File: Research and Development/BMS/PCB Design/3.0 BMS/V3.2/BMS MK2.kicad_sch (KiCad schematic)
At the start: 40 parts, among them J13 CHG VCCs, J4 Batt +, J7 Batt -, J9 CHG GND, Q1 AO3400A, Q2 PN100, Q4 IRF9540N, Q5 IRF9540N, SW1 SW_SPST, SW2 SW_SPST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

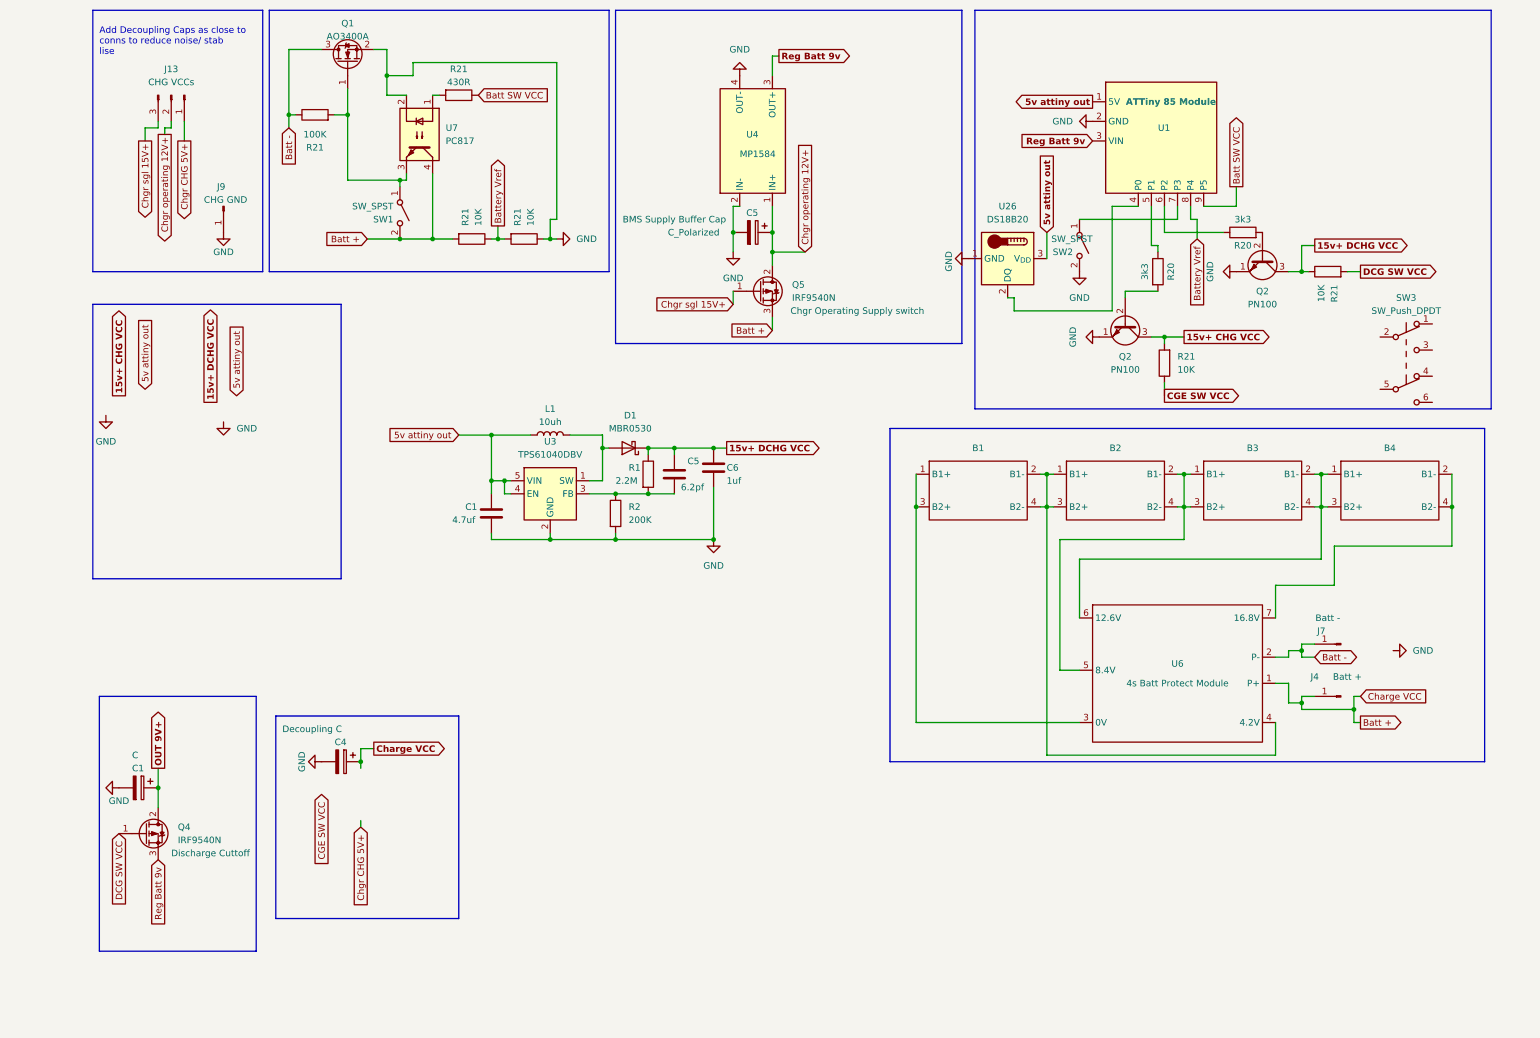
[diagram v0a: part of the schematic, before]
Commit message: Finalised BMS  schematic befeore testing PCB
is rough design without considering guitar dimension, little EMI considerations. not all concepts in design have been ensured to work properly. will test each sections viability before testing entire Circuit.

first design with the batterys and the circuit on the same board. initially had the idea of a 3d printed holder for the cells and a board on top.
 then 3 layers of single sided pcbs triple deckered with smd battery mounts. finally to this style.
although the board is larger in width and length, the height is reduced which should permit a slot in battery design for the guitar rather than a large module with a rail on the side of the guitar for battery to connect to.
This should make the design simpler and will look nicer becasue there will only be a small plastic plate exposed, rather than a chunk of the guitar body being plastic, ruining the over all finish of the guitar.
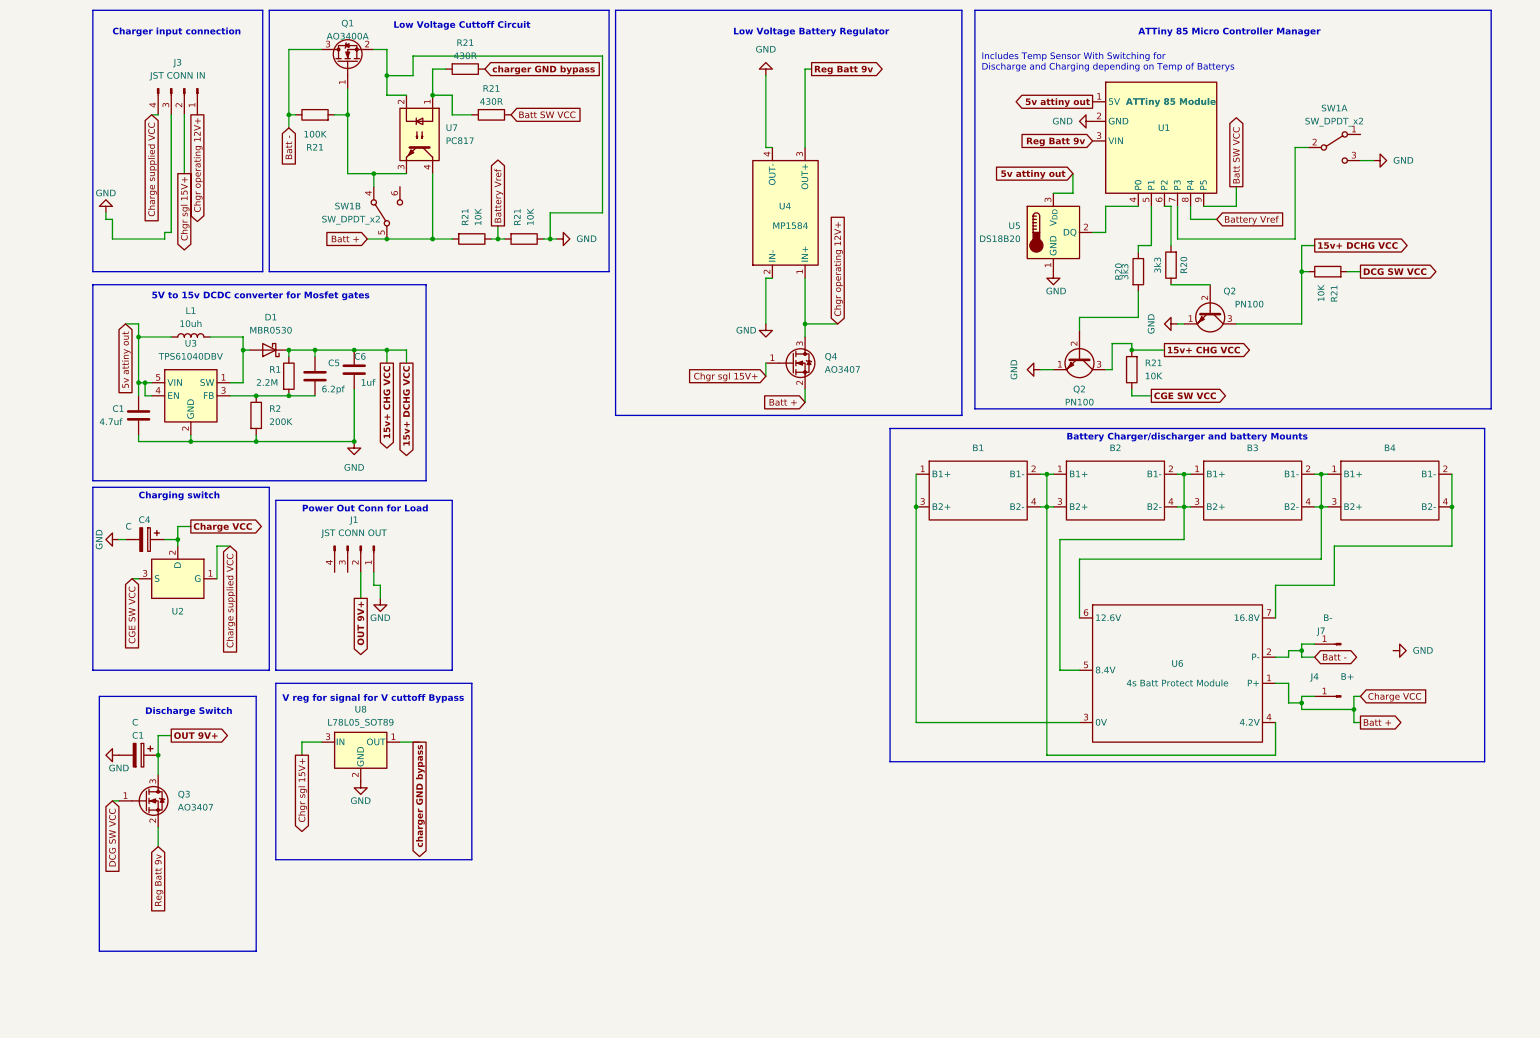
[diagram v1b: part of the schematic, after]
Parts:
- removed C5: C_Polarized, symbol Device:C_Polarized
- removed J13: CHG VCCs, Connector_PinHeader_1.00mm:PinHeader_1x03_P1.00mm_Vertical, symbol Connector:Conn_01x03_Pin
- removed J9: CHG GND, Connector_PinHeader_1.00mm:PinHeader_1x01_P1.00mm_Vertical, symbol Connector:Conn_01x01_Pin
- removed Q4, Q5: IRF9540N, Package_TO_SOT_THT:TO-220-3_Horizontal_TabDown, symbol Transistor_FET:IRF9540N
- removed SW1, SW2: SW_SPST, Button_Switch_THT:SW_PUSH_6mm, symbol Switch:SW_SPST
- removed SW3: SW_Push_DPDT, symbol Switch:SW_Push_DPDT
- removed U26: DS18B20, Package_TO_SOT_THT:TO-92_Inline, symbol Sensor_Temperature:DS18B20
- added J1: JST CONN OUT, Connector_JST:JST_GH_SM04B-GHS-TB_1x04-1MP_P1.25mm_Horizontal, symbol Connector:Conn_01x04_Pin
- added J3: JST CONN IN, Connector_JST:JST_GH_SM04B-GHS-TB_1x04-1MP_P1.25mm_Horizontal, symbol Connector:Conn_01x04_Pin
- added Q3, Q4: AO3407, Package_TO_SOT_SMD:SOT-23, symbol Transistor_FET:AO3400A
- added R21: 430R, Resistor_SMD:R_1206_3216Metric, symbol Device:R
- added SW1: SW_DPDT_x2, Button_Switch_THT:SW_CuK_JS202011CQN_DPDT_Straight, symbol Switch:SW_DPDT_x2
- added U2: ~, Package_TO_SOT_SMD:TO-252-2, symbol BMS-MK2-symbols:AOD409
- added U5: DS18B20, Package_TO_SOT_THT:TO-92_Inline, symbol Sensor_Temperature:DS18B20
- added U8: L78L05_SOT89, Package_TO_SOT_SMD:SOT-89-3, symbol Regulator_Linear:L78L05_SOT89
- B1, B2, B3, B4: footprint (none) -> DCDC buck converter lm2596:18650 Batt 2S Holder
- C4: value Decoupling C -> C
- J4: value Batt + -> B+
- J7: value Batt - -> B-
- U6: footprint (none) -> DCDC buck converter lm2596:BMS 4S Module
- U7: footprint Package_DIP:DIP-4_W7.62mm -> Package_DIP:DIP-4_W8.89mm_SMDSocket_LongPads
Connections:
- net 15v+ DCHG VCC is gone; now on net 15v+ CHG VCC: C5.2, C6.2, D1.1 (K), Q2.3 (C), R1.1, R21.1
- net 5v attiny out: now also U5.3 (V_{DD})
- net Batt +: now also Q4.2 (S), SW1.5 (B), U2.2 (D)
- net CGE SW VCC: now also U2.3 (S)
- net Chgr operating 12V+: now also J3.1 (Pin_1), Q4.3 (D)
- net Chgr sgl 15V+: now also J3.2 (Pin_2), Q4.1 (G), U8.3 (IN)
- net DCG SW VCC: now also Q3.1 (G)
- net GND: now also J1.1 (Pin_1), J3.3 (Pin_3), SW1.3 (C), U5.1 (GND), U8.2 (GND)
- net OUT 9V+ : now also J1.2 (Pin_2), Q3.3 (D)
- net Reg Batt 9v: now also Q3.2 (S)
- net at Q2.2 (B): now also R20.1; no longer R20.2
- net at U1.7 (P3): now also SW1.2 (B)
- net at R21.2, U7.1: now also R21.2
- net at Q1.1 (G), R21.2, U7.3: now also SW1.4 (A)
- net at U1.6 (P2): now also R20.2; no longer R20.1
- net at U1.4 (P0): now also U5.2 (DQ)
- new net Charge supplied VCC: J3.4 (Pin_4), U2.1 (G)
- new net charger GND bypass: R21.1, U8.1 (OUT)
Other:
- note added: "5V to 15v DCDC converter for Mosfet gates"
- note added: "ATTiny 85 Micro Controller Manager"
- note added: "Battery Charger/discharger and battery Mounts"
- note added: "Charger input connection"
- note added: "Charging switch"
- note added: "Discharge Switch"
- note added: "Includes Temp Sensor With Switching for Discharge and Charging depending on Temp of Batterys"
- note added: "Low Voltage Battery Regulator"
- note added: "Low Voltage Cuttoff Circuit"
- note added: "Power Out Conn for Load"
- note added: "V reg for signal for V cuttoff Bypass"
- note removed: "Add Decoupling Caps as close to conns to reduce noise/ stab lise"
- moved on the sheet: C1, C4, C5, C6, D1, L1, Q2, R1, R2, R20, R21, U3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

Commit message: updated bms schem and pcb and added initial schem for charger
fixed charging switch logic for bms board, updated jst conns and now instead uses the supply v as the sw V+ to turn off the mosfet to then charge. should work considering it takes 100ns ~ to switch. added caps in schem but still havent calculated their values, nor are they on the pcb.

created the initial schematic from my notes for a charger that works in respect to the BMS board, is in the same cad file but different sheet to bms and is a seperate pcb.

still need to finalise the caps and also determine pcb via diameters with what i have available and the size requirements. will follow the suggestion for via size from kicad forum
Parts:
- removed J1: JST CONN OUT, Connector_JST:JST_GH_SM04B-GHS-TB_1x04-1MP_P1.25mm_Horizontal, symbol Connector:Conn_01x04_Pin
- removed J3: JST CONN IN, Connector_JST:JST_GH_SM04B-GHS-TB_1x04-1MP_P1.25mm_Horizontal, symbol Connector:Conn_01x04_Pin
- removed U8: L78L05_SOT89, Package_TO_SOT_SMD:SOT-89-3, symbol Regulator_Linear:L78L05_SOT89
- added C4, C7: C, symbol Device:C
- added J1: Conn_01x04_Socket, Connector_JST:JST_GH_SM04B-GHS-TB_1x04-1MP_P1.25mm_Horizontal, symbol Connector:Conn_01x04_Socket
- added J5: CHG IN, Connector_JST:JST_GH_SM04B-GHS-TB_1x04-1MP_P1.25mm_Horizontal, symbol Connector:Conn_01x04_Socket
- R21: value 430R -> 1.8K
- renumbered J4 to TP1, J7 to TP2
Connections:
- net Chgr operating 12V+ is gone; now on net +VDC: Q4.3 (D), U4.1 (IN+)
- net DCG SW VCC is gone; now on net CGE SW V+: Q3.1 (G), R21.2
- net charger GND bypass is gone; now on net +VDC: R21.1
- net 5v attiny out: now also C4.2
- net Battery Vref: now also J1.3 (Pin_3), J5.1 (Pin_1)
- net GND: now also C4.1, J1.1 (Pin_1), J5.4 (Pin_4)
- net OUT 9V+ : now also J1.2 (Pin_2)
- net at R21.2, U7.1: no longer R21.2
- net Batt + renamed +BATT
- net Batt - renamed -BATT
- net -BATT: now also C7.1, J5.2 (Pin_2)
- net CGE SW VCC renamed CGE SW V+
- net Charge supplied VCC renamed +VDC
- net +VDC: now also C7.2, J5.3 (Pin_3)
- net Chgr sgl 15V+: no longer names the net of Q4.1 (G)
- net Chgr sgl 15V+: now also R21.2
- net Reg Batt 9v renamed +9V
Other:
- removed sheet Battery charging block
- removed sheet Charger 
- added sheet Charger (untitled.kicad_sch)
- note removed: "V reg for signal for V cuttoff Bypass"
- moved on the sheet: Q4, TP1, TP2, U4
